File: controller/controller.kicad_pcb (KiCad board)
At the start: 4 copper layers, 85 x 39 mm, 100 parts, among them J1 Conn_01x14, J2 Conn_01x14, J3 Conn_01x14, J4 Conn_01x14, J5 Conn_01x14, J6 USB_C_Receptacle_USB2.0_16P, J7 USB_C_Receptacle_PowerOnly_6P, J8 Conn_01x03_Pin, J9 Conn_01x03_Pin, U1 STM32G474RCTx, U2 LM5168, U3 TLV76133DCY, U4 TLV76150DCY, U6 STM32G474VETx, U7 STM32G474METx

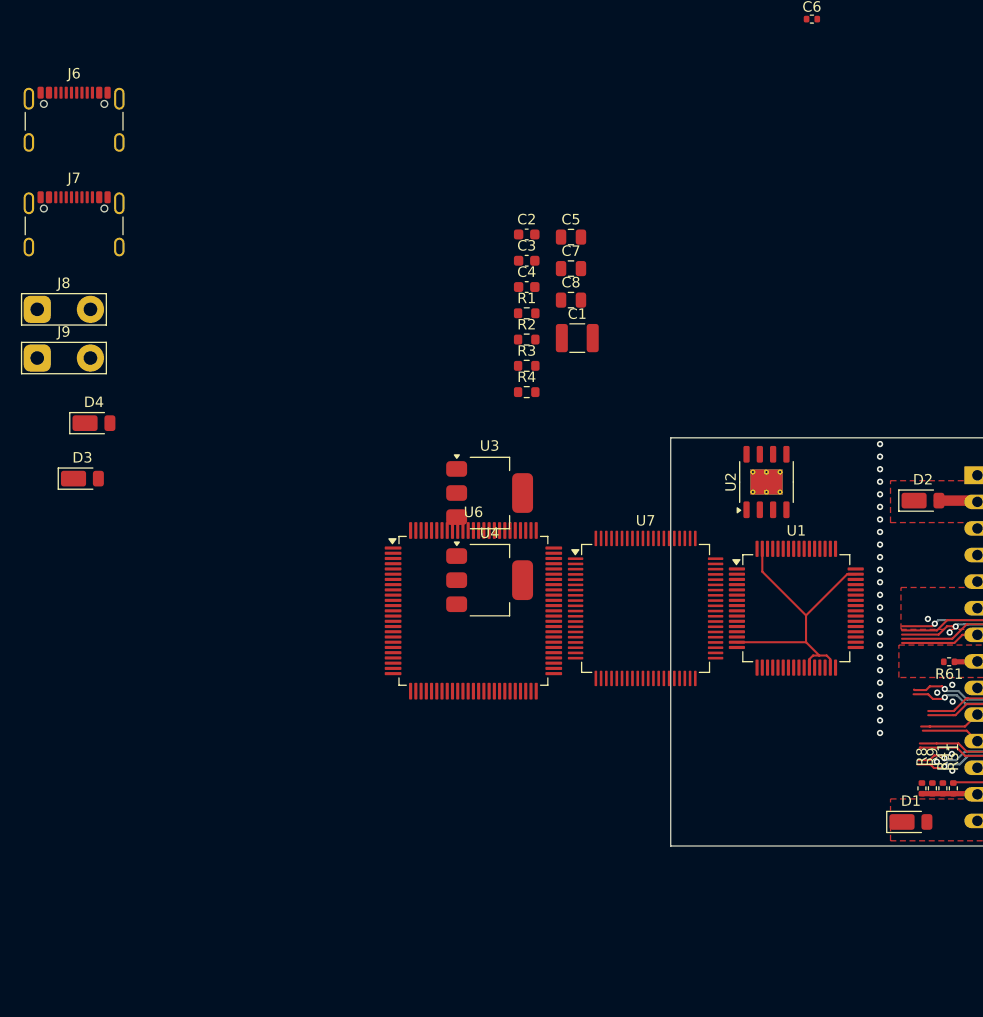
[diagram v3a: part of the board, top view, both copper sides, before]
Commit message: More work on controller - Add decoupling caps for mcu etc
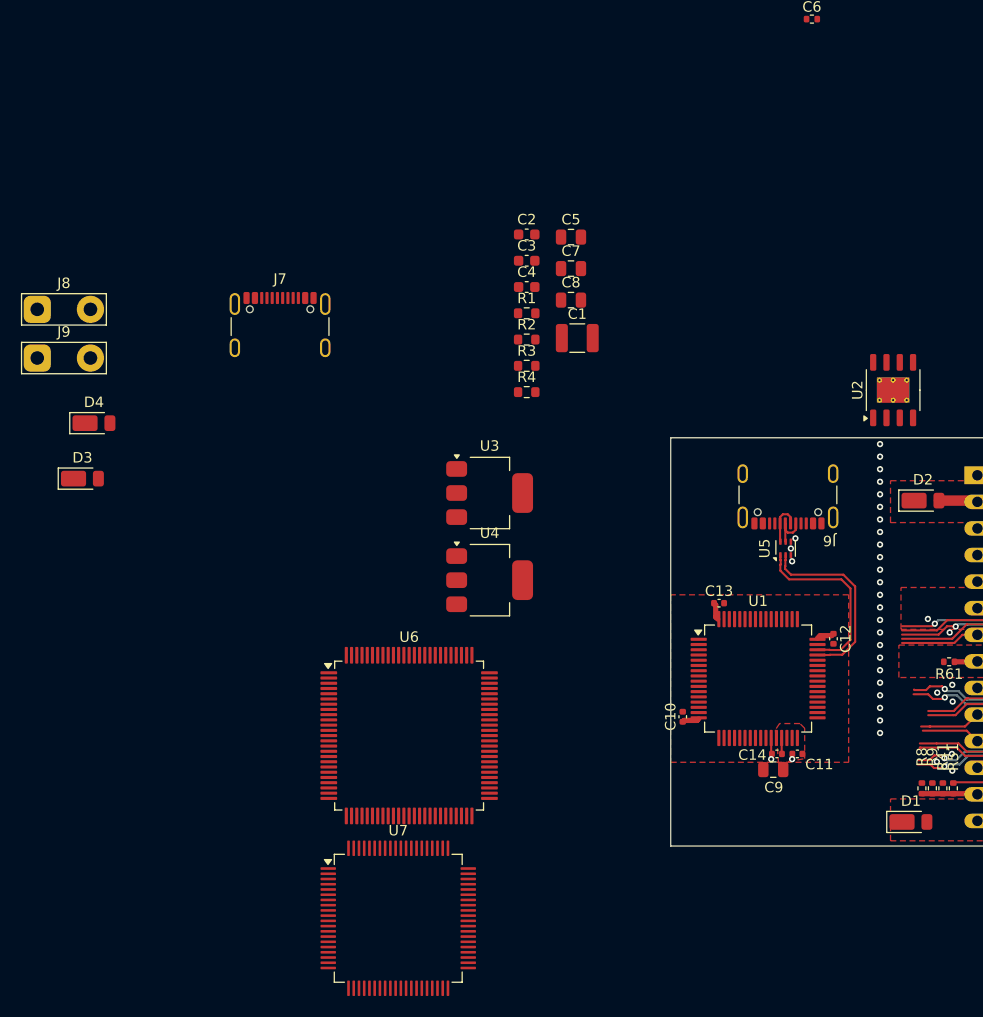
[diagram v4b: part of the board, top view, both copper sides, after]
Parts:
- added C10: 100nF, Capacitor_SMD:C_0402_1005Metric, F.Cu at (86.2, 91.7)
- added C11: 100nF, Capacitor_SMD:C_0402_1005Metric, F.Cu at (97.1, 95.2)
- added C12: 100nF, Capacitor_SMD:C_0402_1005Metric, F.Cu at (100.5, 84.2)
- added C13: 100nF, Capacitor_SMD:C_0402_1005Metric, F.Cu at (89.6, 80.8)
- added C14: 100nF, Capacitor_SMD:C_0402_1005Metric, F.Cu at (95.2, 95.2)
- added C9: 4.7uF, Capacitor_SMD:C_0805_2012Metric, F.Cu at (94.8, 96.7)
- added U5: ECMF02-2AMX6, Package_DFN_QFN:ST_UQFN-6L_1.5x1.7mm_P0.5mm, F.Cu at (96.0, 75.6)
- moved J6 76.1 mm to (96.2, 69.5), turned to 180 degrees
- moved U7 37.9 mm to (59.0, 110.9)
- moved J7 21.9 mm to (47.7, 55.3)
- moved U2 14.9 mm to (106.2, 60.4)
- moved U6 13.4 mm to (60.0, 93.5)
- moved U1 7.65 mm to (93.3, 88.0)
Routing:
- net Earth: track 30.5 -> 2.69 mm, vias 32 -> 37
- net USB_D-: track 0.00 -> 18.1 mm
- net USB_D+: track 0.00 -> 17.4 mm
- net +3V3: track 0.00 -> 6.56 mm
- net Net-(U5-D_OUT-): track 0.00 -> 4.26 mm
- net Net-(U5-D_OUT+): track 0.00 -> 4.19 mm
- added copper zone on F.Cu, net +3V3
- added copper zone on F.Cu, net Earth

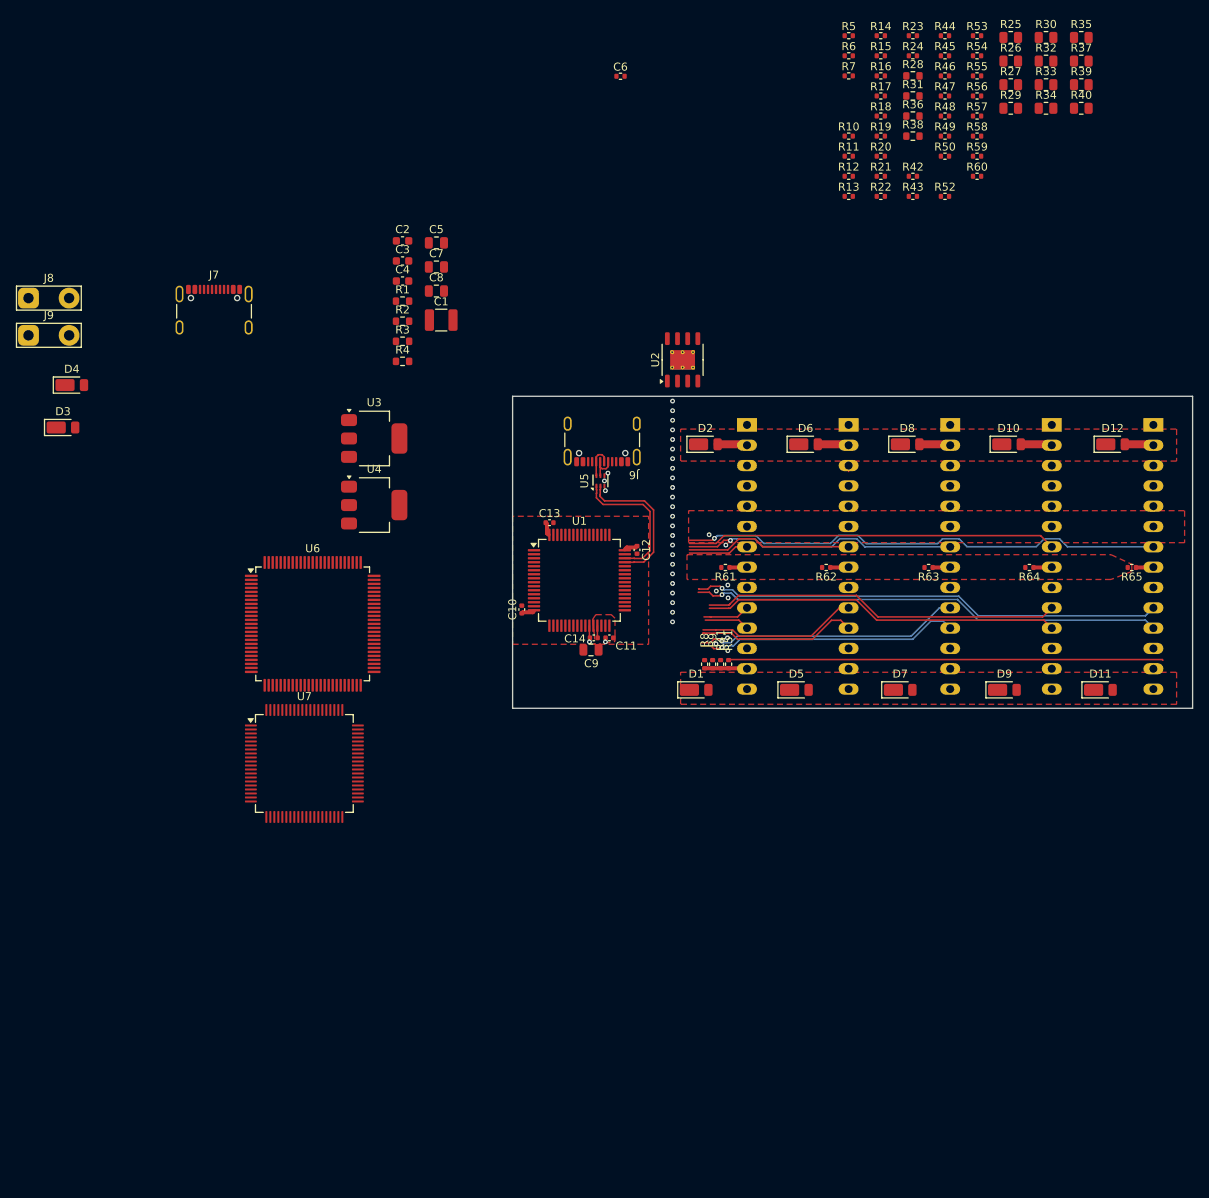
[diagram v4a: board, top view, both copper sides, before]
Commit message: Add wifi module
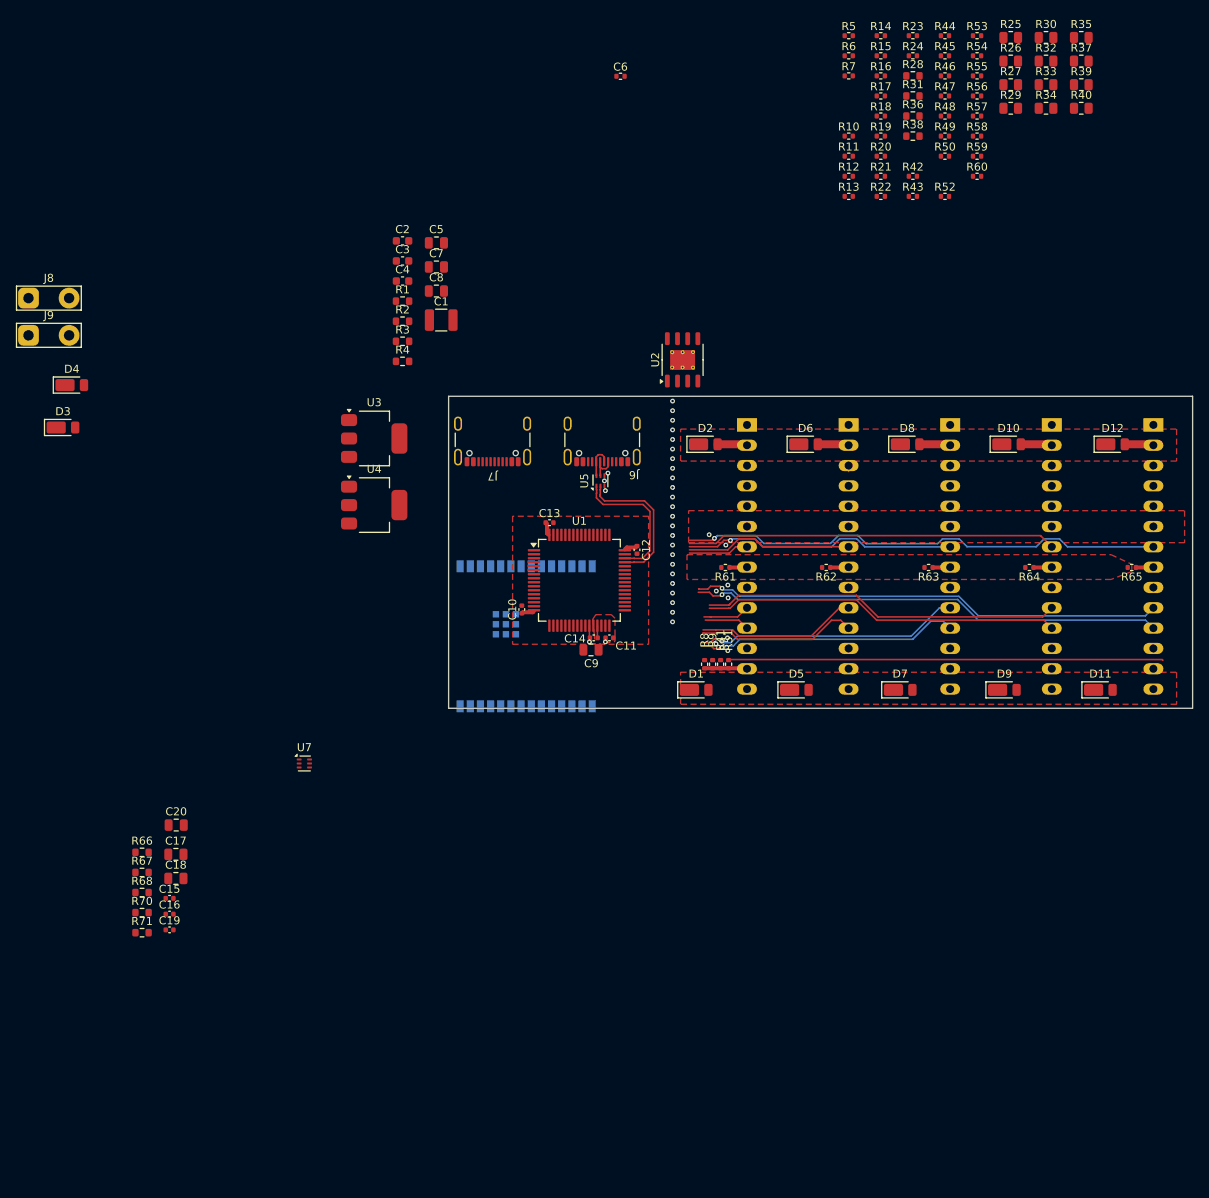
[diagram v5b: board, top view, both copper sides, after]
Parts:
- added C15: 100nF, Capacitor_SMD:C_0402_1005Metric, F.Cu at (42.1, 127.8)
- added C16: 100nF, Capacitor_SMD:C_0402_1005Metric, F.Cu at (42.1, 129.7)
- added C17: 10uF, Capacitor_SMD:C_0805_2012Metric, F.Cu at (42.9, 122.3)
- added C18: 10uF, Capacitor_SMD:C_0805_2012Metric, F.Cu at (42.9, 125.3)
- added C19: 100nF, Capacitor_SMD:C_0402_1005Metric, F.Cu at (42.1, 131.7)
- added C20: 10uF, Capacitor_SMD:C_0805_2012Metric, F.Cu at (43.0, 118.6)
- added R66: 10k, Resistor_SMD:R_0603_1608Metric, F.Cu at (38.7, 122.0)
- added R67: 10k, Resistor_SMD:R_0603_1608Metric, F.Cu at (38.7, 124.5)
- added R68: 10k, Resistor_SMD:R_0603_1608Metric, F.Cu at (38.7, 127.0)
- added R70: 1k, Resistor_SMD:R_0603_1608Metric, F.Cu at (38.7, 129.5)
- added R71: 1k, Resistor_SMD:R_0603_1608Metric, F.Cu at (38.7, 132.1)
- C9: value 4.7uF -> 10uF
- J7: value USB_C_Receptacle_PowerOnly_6P -> USB_C_Receptacle_USB2.0_16P
- U6: value STM32G474VETx -> ESP32-C6-WROOM-1; footprint Package_QFP:LQFP-100_14x14mm_P0.5mm -> Library:ESP32-C6-WROOM-1; moved to B.Cu
- U7: value STM32G474METx -> ECMF02-2AMX6; footprint Package_QFP:LQFP-80_12x12mm_P0.5mm -> Package_DFN_QFN:ST_UQFN-6L_1.5x1.7mm_P0.5mm
- moved J7 37.6 mm to (82.5, 69.5), turned to 180 degrees
- moved U6 26.7 mm to (86.7, 95.0), turned to -90 degrees
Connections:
- J7 pad A1: (no net) -> Earth
- J7 pad A4: (no net) -> Net-(D4-A)
- J7 pad A6: (no net) -> Net-(U7-D_OUT+)
- J7 pad A7: (no net) -> Net-(U7-D_OUT-)
- J7 pad A8: (no net) -> unconnected-(J7-SBU1-PadA8)
- J7 pad B1: (no net) -> Earth
- J7 pad B4: (no net) -> Net-(D4-A)
- J7 pad B6: (no net) -> Net-(U7-D_OUT+)
- J7 pad B7: (no net) -> Net-(U7-D_OUT-)
- J7 pad B8: (no net) -> unconnected-(J7-SBU2-PadB8)
- J9 pad 1: FB_LOW -> unconnected-(J9-Pin_1-Pad1)
- U1 pad 22: unconnected-(U1-PC4-Pad22) -> /STM32_TX
- U1 pad 23: HRTIM1_EEV10 -> /STM32_RX
- U1 pad 61: BOOT0 -> /STM32_BOOT0
- U1 pad 7: unconnected-(U1-PG10-Pad7) -> Net-(U1-PG10)
- U6 pad 1: unconnected-(U6-PE2-Pad1) -> Earth
- U6 pad 10: unconnected-(U6-PF9-Pad10) -> Net-(U6-GPIO8)
- U6 pad 13: unconnected-(U6-PF1-Pad13) -> ESP_USB_D-
- U6 pad 14: unconnected-(U6-PG10-Pad14) -> ESP_USB_D+
- U6 pad 15: unconnected-(U6-PC0-Pad15) -> Net-(U6-GPIO9)
- U6 pad 18: unconnected-(U6-PC3-Pad18) -> /STM32_BOOT0
- U6 pad 19: unconnected-(U6-PF2-Pad19) -> /STM32_NRST
- U6 pad 2: unconnected-(U6-PE3-Pad2) -> +3V3
- U6 pad 20: unconnected-(U6-PA0-Pad20) -> /STM32_TX
- U6 pad 21: unconnected-(U6-PA1-Pad21) -> /STM32_RX
- U6 pad 23: Net-(U6-VSS-Pad23) -> unconnected-(U6-GPIO15-Pad23)
- U6 pad 28: unconnected-(U6-PA6-Pad28) -> Earth
- U6 pad 29: unconnected-(U6-PA7-Pad29) -> Earth
- U6 pad 3: unconnected-(U6-PE4-Pad3) -> Net-(U6-EN/CHIP_PU)
- U6 pad 4: unconnected-(U6-PE5-Pad4) -> Net-(J10-SWDIO/TMS)
- U6 pad 5: unconnected-(U6-PE6-Pad5) -> Net-(J10-NC/TDI)
- U6 pad 6: unconnected-(U6-VBAT-Pad6) -> Net-(J10-SWCLK/TCK)
- U6 pad 7: unconnected-(U6-PC13-Pad7) -> Net-(J10-SWO/TDO)
- U7 pad 1: unconnected-(U7-VBAT-Pad1) -> ESP_USB_D+
- U7 pad 2: unconnected-(U7-PC13-Pad2) -> ESP_USB_D-
- U7 pad 3: unconnected-(U7-PC14-Pad3) -> Earth
- U7 pad 4: unconnected-(U7-PC15-Pad4) -> Earth
- U7 pad 5: unconnected-(U7-PF0-Pad5) -> Net-(U7-D_OUT-)
- U7 pad 6: unconnected-(U7-PF1-Pad6) -> Net-(U7-D_OUT+)
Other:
- board size 85 x 39 mm -> 93 x 39 mm

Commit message: Controller - Lots of changes
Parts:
- added C21: 100nF, Capacitor_SMD:C_0402_1005Metric, F.Cu at (74.0, 153.5)
- added C22: 100nF, Capacitor_SMD:C_0402_1005Metric, F.Cu at (74.0, 155.5)
- added C23: 100nF, Capacitor_SMD:C_0402_1005Metric, F.Cu at (74.0, 157.5)
- added C24: 100nF, Capacitor_SMD:C_0402_1005Metric, F.Cu at (74.0, 159.4)
- added C25: ?, Capacitor_SMD:C_0603_1608Metric, B.Cu at (88.7, 74.9)
- added D13: BAT54S, Package_TO_SOT_SMD:SOT-23, F.Cu at (57.4, 141.0)
- added D14: BAT54S, Package_TO_SOT_SMD:SOT-23, F.Cu at (57.4, 145.7)
- added D15: BAT54S, Package_TO_SOT_SMD:SOT-23, F.Cu at (57.4, 150.3)
- added D16: BAT54S, Package_TO_SOT_SMD:SOT-23, F.Cu at (57.4, 154.9)
- added D17: BAT54S, Package_TO_SOT_SMD:SOT-23, F.Cu at (57.4, 159.5)
- added D18: BAT54S, Package_TO_SOT_SMD:SOT-23, F.Cu at (62.3, 141.0)
- added D19: BAT54S, Package_TO_SOT_SMD:SOT-23, F.Cu at (62.3, 145.7)
- added D20: BAT54S, Package_TO_SOT_SMD:SOT-23, F.Cu at (62.3, 150.3)
- added D21: BAT54S, Package_TO_SOT_SMD:SOT-23, F.Cu at (62.3, 154.9)
- added D22: BAT54S, Package_TO_SOT_SMD:SOT-23, F.Cu at (62.3, 159.5)
- added L1: 180uH 630mOhm, duger LQH55DN151M03L?, Inductor_SMD:L_Murata_LQH55DN_5.7x5.0mm, B.Cu at (84.0, 69.8)
- added R72: 0R, Resistor_SMD:R_0402_1005Metric, F.Cu at (66.2, 139.6)
- added R73: 1k, Resistor_SMD:R_0603_1608Metric, F.Cu at (74.5, 161.7)
- added R74: 0R, Resistor_SMD:R_0402_1005Metric, F.Cu at (66.2, 141.6)
- added R75: 0R, Resistor_SMD:R_0402_1005Metric, F.Cu at (66.2, 143.6)
- added R76: 0R, Resistor_SMD:R_0402_1005Metric, F.Cu at (66.2, 145.6)
- added R77: 0R, Resistor_SMD:R_0402_1005Metric, F.Cu at (66.2, 147.6)
- added R78: 0R, Resistor_SMD:R_0402_1005Metric, F.Cu at (66.2, 149.6)
- added R79: 0R, Resistor_SMD:R_0402_1005Metric, F.Cu at (66.2, 151.6)
- added R80: 0R, Resistor_SMD:R_0402_1005Metric, F.Cu at (69.1, 139.6)
- added R81: 0R, Resistor_SMD:R_0402_1005Metric, F.Cu at (69.1, 141.6)
- added R82: 0R, Resistor_SMD:R_0402_1005Metric, F.Cu at (69.1, 143.6)
- added R83: 0R, Resistor_SMD:R_0402_1005Metric, F.Cu at (69.1, 145.6)
- added R84: 0R, Resistor_SMD:R_0402_1005Metric, F.Cu at (69.1, 147.6)
- added R85: 0R, Resistor_SMD:R_0402_1005Metric, F.Cu at (69.1, 149.6)
- added R86: 0R, Resistor_SMD:R_0402_1005Metric, F.Cu at (69.1, 151.6)
- added R87: 0R, Resistor_SMD:R_0402_1005Metric, F.Cu at (72.0, 139.6)
- added R88: 0R, Resistor_SMD:R_0402_1005Metric, F.Cu at (72.0, 141.6)
- added R89: 0R, Resistor_SMD:R_0402_1005Metric, F.Cu at (72.0, 143.6)
- added R90: 0R, Resistor_SMD:R_0402_1005Metric, F.Cu at (72.0, 145.6)
- added R91: 0R, Resistor_SMD:R_0402_1005Metric, F.Cu at (72.0, 147.6)
- added R92: 0R, Resistor_SMD:R_0402_1005Metric, F.Cu at (72.0, 149.6)
- added R93: 0R, Resistor_SMD:R_0402_1005Metric, F.Cu at (72.0, 151.6)
- added R94: 0R, Resistor_SMD:R_0402_1005Metric, F.Cu at (75.0, 139.6)
- added R95: 0R, Resistor_SMD:R_0402_1005Metric, F.Cu at (75.0, 141.6)
- added R96: 0R, Resistor_SMD:R_0402_1005Metric, F.Cu at (75.0, 143.6)
- added R98: ?, Resistor_SMD:R_0603_1608Metric, B.Cu at (85.6, 74.9)
- added U8: TS3011IYLT, Package_TO_SOT_SMD:SOT-23-5, F.Cu at (67.3, 161.6)
- added U9: PY32F002AA15M, Package_SO:SSOP-10_3.9x4.9mm_P1.00mm, F.Cu at (68.6, 156.0)
- C1, C2, C3, C4, C8, R1, R2, R3, R4, U2, U4: moved to B.Cu
- C5: footprint Capacitor_SMD:C_0805_2012Metric -> Capacitor_SMD:C_1206_3216Metric; moved to B.Cu
- C6: footprint Resistor_SMD:R_0402_1005Metric -> Capacitor_SMD:C_0603_1608Metric; moved to B.Cu
- moved C6 52.6 mm to (91.8, 77.1), turned to 90 degrees
- moved U7 42.3 mm to (82.3, 75.6), turned to 90 degrees
- moved U4 41.0 mm to (108.4, 83.2), turned to -90 degrees
- moved C8 40.8 mm to (107.1, 77.7), turned to 180 degrees
- moved C2 33.7 mm to (82.8, 77.2), turned to 90 degrees
- moved C4 32.4 mm to (80.4, 81.6)
- moved R4 29.3 mm to (91.8, 81.6), turned to -90 degrees
- moved C1 28.5 mm to (94.2, 77.4), turned to 90 degrees
- moved U3 28.4 mm to (40.3, 77.7)
- moved C5 28.1 mm to (88.5, 70.7), turned to -90 degrees
- moved U2 26.2 mm to (87.2, 78.4), turned to 180 degrees
- moved R2 26.1 mm to (80.4, 80.0)
- moved R3 25.5 mm to (82.7, 80.8), turned to -90 degrees
- moved C3 23.0 mm to (80.1, 69.3), turned to -90 degrees
- moved R1 21.2 mm to (80.5, 72.2), turned to 90 degrees
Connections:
- net /STM32_NRST renamed /STM32_NRST_TO_ESP
- net FB_D renamed /FB_D
- J1 pad 3: Earth -> /Current_sense_1B
- J1 pad 4: Current_sense_1 -> /Current_sense_1A
- J1 pad 7: NTC_1 -> /NTC_1
- J2 pad 3: Earth -> /Current_sense_2B
- J2 pad 4: Current_sense_2 -> /Current_sense_2A
- J2 pad 7: NTC_2 -> /NTC_2
- J3 pad 3: Earth -> /Current_sense_3B
- J3 pad 4: Current_sense_3 -> /Current_sense_3A
- J3 pad 7: NTC_3 -> /NTC_3
- J4 pad 3: Earth -> /Current_sense_4B
- J4 pad 4: Current_sense_4 -> /Current_sense_4A
- J4 pad 7: NTC_4 -> /NTC_4
- J5 pad 3: Earth -> /Current_sense_5B
- J5 pad 4: Current_sense_5 -> /Current_sense_5A
- J5 pad 7: NTC_5 -> /NTC_5
- R25 pad 2: FB_A -> /FB_A
- R26 pad 2: FB_A -> /FB_A
- R27 pad 2: FB_A -> /FB_A
- R28 pad 1: FB_A -> /FB_A
- R29 pad 2: FB_B -> /FB_B
- R30 pad 2: FB_B -> /FB_B
- R31 pad 1: FB_B -> /FB_B
- R32 pad 2: FB_B -> /FB_B
- R33 pad 2: FB_C -> /FB_C
- R35 pad 2: FB_C -> /FB_C
- R36 pad 1: FB_C -> /FB_C
- R39 pad 2: FB_C -> /FB_C
- U1 pad 11: OPAMP5_VINP -> /FB_C
- U1 pad 12: COMP3_INP -> /Current_sense_5
- U1 pad 13: OPAMP1_VINP -> /FB_A
- U1 pad 17: COMP2_INP -> /Current_sense_1A
- U1 pad 18: unconnected-(U1-PA4-Pad18) -> /Current_sense_5_ref
- U1 pad 20: unconnected-(U1-PA6-Pad20) -> /Current_sense_5_ref
- U1 pad 21: OPAMP2_VINP -> /FB_B
- U1 pad 24: COMP4_INP -> /Current_sense_2A
- U1 pad 25: COMP1_INP -> /Current_sense_4
- U1 pad 26: unconnected-(U1-PB2-Pad26) -> Net-(U1-PB2)
- U1 pad 34: HRTIM1_CHC1 -> /HI_2
- U1 pad 35: HRTIM1_CHC2 -> /LI_2
- U1 pad 36: HRTIM1_CHD1 -> Net-(D18-COM)
- U1 pad 37: HRTIM1_CHD2 -> Net-(U1-PB15)
- U1 pad 38: HRTIM1_CHF1 -> /HI_1
- U1 pad 39: HRTIM1_CHF2 -> /LI_1
- U1 pad 40: HRTIM1_CHE1 -> /HI_3
- U1 pad 41: HRTIM1_CHE2 -> /LI_3
- U1 pad 42: HRTIM1_CHA1 -> /HI_4
- U1 pad 49: unconnected-(U1-PA13-Pad49) -> /STM32_SWDIO
- U1 pad 50: unconnected-(U1-PA14-Pad50) -> /STM32_SWC
- U1 pad 8: unconnected-(U1-PC0-Pad8) -> Net-(U1-PC0)
- U1 pad 9: COMP3_INP -> Net-(U1-PC1)
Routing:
- net NTC_5: track 61.0 -> 0.00 mm, vias 1 -> 0
- net /NTC_5: track 0.00 -> 61.0 mm, vias 0 -> 1
- net 6-18V: track 0.00 -> 60.6 mm, vias 0 -> 2
- net NTC_4: track 46.3 -> 0.00 mm
- net /NTC_4: track 0.00 -> 46.3 mm
- net NTC_3: track 34.6 -> 0.00 mm, vias 1 -> 0
- net /NTC_3: track 0.00 -> 34.6 mm, vias 0 -> 1
- net NTC_2: track 20.9 -> 0.00 mm
- net /NTC_2: track 0.00 -> 20.9 mm
- net Net-(C3-Pad2): track 0.00 -> 13.9 mm, vias 0 -> 2
- net NTC_1: track 7.52 -> 0.00 mm
- net /NTC_1: track 0.00 -> 7.52 mm
- net Net-(U2-SW): track 0.00 -> 7.37 mm
- net Net-(U2-FB): track 0.00 -> 5.66 mm
- net Net-(U7-D_OUT+): track 0.00 -> 4.24 mm
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- added copper zone on B.Cu, net +5V
- added copper zone on B.Cu, net 6-18V
- added copper zone on B.Cu, net Logic DC/DC in
- added copper zone on B.Cu, net Net-(U2-SW)
